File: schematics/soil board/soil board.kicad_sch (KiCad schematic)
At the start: 20 parts, among them J1 AVR-ISP-6, U1 ATtiny841-SS, U3 MCP9700Ax-ETT

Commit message: rough draft for a board with capcitive sensor and soil temp sensor, can use rs-485 to communicate
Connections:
- net floating is gone; now on net CAP_CHARGE: Elecctrodes1.2
- net CAP_CHARGE: no longer Elecctrodes1.1
- net GND: now also Elecctrodes1.1
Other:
- moved on the sheet: Elecctrodes1
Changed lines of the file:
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@@
-	(wire
-		(pts
-			(xy 162.56 85.09) (xy 168.91 85.09)
-		)
-		(stroke
-			(width 0)
-			(type default)
-		)
-	)
 	(wire
 		(pts
@@
 		(property "Intersheetrefs" "${INTERSHEET_REFS}"
 			(at 98.0537 107.95 0)
-			(hide yes)
-			(show_name no)
-			(do_not_autoplace no)
-			(effects
-				(font
-					(size 1.27 1.27)
-				)
-				(justify left)
-			)
-		)
-	)
-	(global_label "floating"
-		(shape input)
-		(at 168.91 85.09 0)
-		(fields_autoplaced yes)
-		(effects
-			(font
-				(size 1.27 1.27)
-			)
-			(justify left)
-		)
-		(property "Intersheetrefs" "${INTERSHEET_REFS}"
-			(at 179.2126 85.09 0)
 			(hide yes)
 			(show_name no)
@@
 	(symbol
 		(lib_id "Device:C")
-		(at 158.75 85.09 90)
+		(at 158.75 85.09 270)
 		(unit 1)
 		(body_style 1)
@@
 		)
 		(property "Footprint" "soil_cap:Untitled"
-			(at 162.56 84.1248 0)
+			(at 154.94 86.0552 0)
 			(hide yes)
 			(show_name no)
@@
 					(unit 1)
 				)
+			)
+		)
+	)
+	(symbol
+		(lib_id "power:GND")
+		(at 162.56 85.09 0)
+		(unit 1)
+		(body_style 1)
+		(exclude_from_sim no)
+		(in_bom yes)
+		(on_board yes)
+		(in_pos_files yes)
+		(dnp no)
+		(fields_autoplaced yes)
+		(property "Reference" "#PWR09"
+			(at 162.56 91.44 0)
+			(hide yes)
+			(show_name no)
+			(do_not_autoplace no)
+			(effects
+				(font
+					(size 1.27 1.27)
+				)
+			)
+		)
+		(property "Value" "GND"
+			(at 162.56 90.17 0)
+			(show_name no)
+			(do_not_autoplace no)
+			(effects
+				(font
+					(size 1.27 1.27)
+				)
+			)
+		)
+		(property "Footprint" ""
+			(at 162.56 85.09 0)
+			(hide yes)
+			(show_name no)
+			(do_not_autoplace no)
+			(effects
+				(font
+					(size 1.27 1.27)
+				)
+			)
+		)
+		(property "Datasheet" ""
+			(at 162.56 85.09 0)
+			(hide yes)
+			(show_name no)
+			(do_not_autoplace no)
+			(effects
+				(font
+					(size 1.27 1.27)
+				)
+			)
+		)
+		(property "Description" "Power symbol creates a global label with name \"GND\" , ground"
+			(at 162.56 85.09 0)
+			(hide yes)
+			(show_name no)
+			(do_not_autoplace no)
+			(effects
+				(font
+					(size 1.27 1.27)
+				)
+			)
+		)
+		(pin "1"
+		)
+		(instances
+			(project "soil board"
+				(path "/37916b7e-9322-4a41-838c-6f1f6ef59153"
+					(reference "#PWR09")
+					(unit 1)
+				)

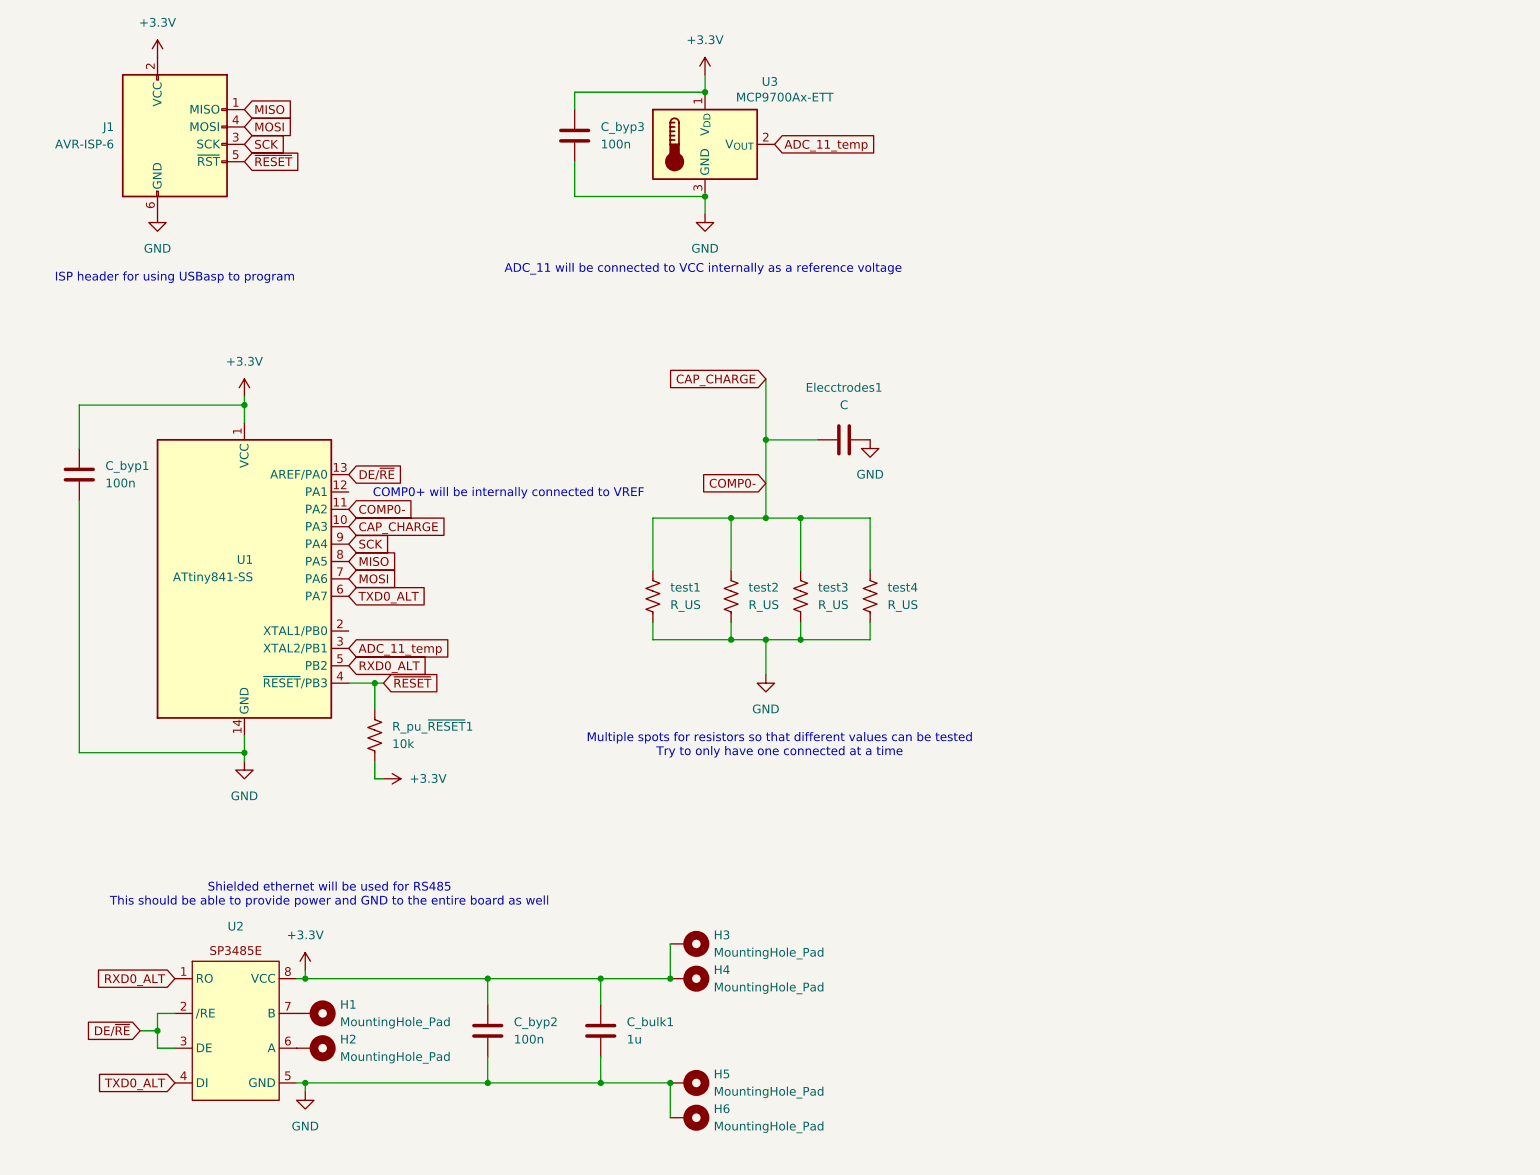
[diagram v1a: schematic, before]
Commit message: Changed connectors for rs-485
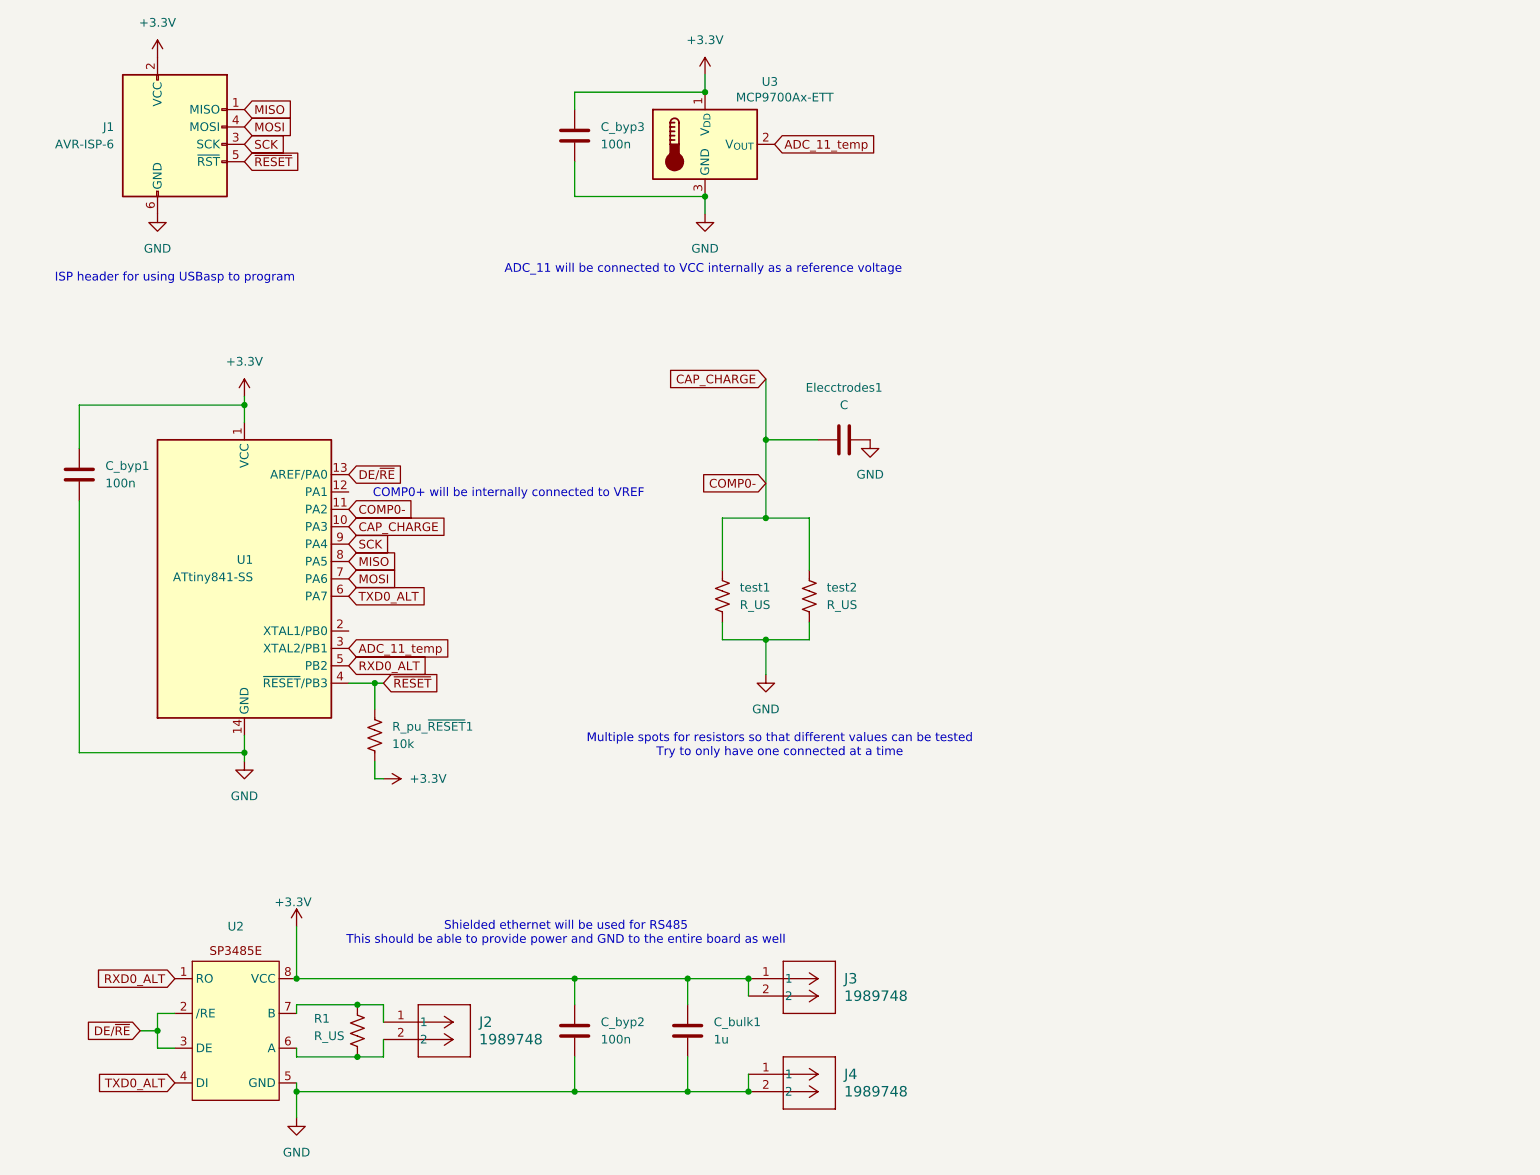
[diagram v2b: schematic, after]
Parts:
- removed H1, H2, H3, H4, H5, H6: MountingHole_Pad, Connector_Wire:SolderWire-0.5sqmm_1x01_D0.9mm_OD2.1mm, symbol Mechanical:MountingHole_Pad
- removed test3, test4: R_US, Resistor_THT:R_Axial_DIN0207_L6.3mm_D2.5mm_P7.62mm_Horizontal, symbol Device:R_US
- added J2: 1989748, footprints:CONN_1989748_PXC, symbol 2026-10-16_21-18-38:1989748
- added J3, J4: 1989748, CONN_1989748_PXC, symbol 2026-10-16_21-18-38:1989748
- added R1: R_US, Resistor_SMD:R_0805_2012Metric_Pad1.20x1.40mm_HandSolder, symbol Device:R_US
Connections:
- net +3.3V: now also J3.1, J3.2
- net GND: now also J4.1, J4.2
- net at U2.7 (B): now also J2.1, R1.1
- net at U2.6 (A): now also J2.2, R1.2
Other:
- moved on the sheet: C_bulk1, C_byp2, test1, test2

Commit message: Interface for temp sensor and soil moisture sensor
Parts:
- removed Elecctrodes1: C, soil_cap:Untitled, symbol Device:C
- removed J2: 1989748, footprints:CONN_1989748_PXC, symbol 2026-10-16_21-18-38:1989748
- removed J3, J4: 1989748, CONN_1989748_PXC, symbol 2026-10-16_21-18-38:1989748
- removed test1, test2: R_US, Resistor_THT:R_Axial_DIN0207_L6.3mm_D2.5mm_P7.62mm_Horizontal, symbol Device:R_US
- added J2: Conn_01x03_Pin, Connector_PinHeader_2.54mm:PinHeader_1x03_P2.54mm_Vertical, symbol Connector:Conn_01x03_Pin
- added J5: 54602-908LF, CONN8_2-908LF_AMP, symbol 2026-10-21_23-02-14:54602-908LF
- added PWR1, TEST1: LED, LED_SMD:LED_0805_2012Metric_Pad1.15x1.40mm_HandSolder, symbol Device:LED
- added R2, R3: 56, Resistor_SMD:R_0805_2012Metric_Pad1.20x1.40mm_HandSolder, symbol Device:R_US
- R1: value R_US -> 120
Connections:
- net +3.3V: now also J2.3 (Pin_3), J5.7, J5.8, PWR1.2 (A)
- net ADC_11_temp: now also U1.2 (XTAL1/PB0); no longer U1.3 (XTAL2/PB1)
- net GND: now also J2.1 (Pin_1), J5.1, J5.2, R2.2, R3.2
- net /RE: now reaches U1.12 (PA1)
- net /RE: now also U2.2 (/RE)
- net at R1.2, U2.6 (A): now also J5.4
- net at R1.1, U2.7 (B): now also J5.5
- net CAP_CHARGE: no longer names the net of U1.11 (PA2)
- net CAP_CHARGE: now also TEST1.2 (A); no longer U1.10 (PA3)
- net DE/~{RE} renamed DE
- net DE: no longer U2.2 (/RE)
- new net: PWR1.1 (K), R2.1
- new net: R3.1, TEST1.1 (K)
- new net ADC_10_moisture: J2.2 (Pin_2), U1.3 (XTAL2/PB1)
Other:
- note added: "Interface with soil moisture Sensor"
- note added: "Place near the RJ45 jack"
- note removed: "COMP0+ will be internally connected to VREF"
- note removed: "Multiple spots for resistors so that different values can be tested Try to only have one connected at a time"
- moved on the sheet: C_bulk1, C_byp1, C_byp2, R1, R_pu_~{RESET}1, U1, U2

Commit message: Final changes to pcbs before ordering
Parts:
- renumbered C_bulk1 to C1, C_byp1 to C2, C_byp2 to C3, C_byp3 to C4, J5 to J2, J2 to J3, R_pu_~{RESET}1 to R1, R3 to R2, R2 to R3, R1 to R4
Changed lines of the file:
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@@
 		(in_pos_files yes)
 		(dnp no)
-		(property "Reference" "R2"
+		(property "Reference" "R3"
 			(at 166.37 134.112 0)
 			(show_name no)
@@
 			(project "soil board"
 				(path "/37916b7e-9322-4a41-838c-6f1f6ef59153"
-					(reference "R2")
+					(reference "R3")
 					(unit 1)
 				)
@@
 		(dnp no)
 		(fields_autoplaced yes)
-		(property "Reference" "R_pu_~{RESET}1"
+		(property "Reference" "R1"
 			(at 88.9 132.0799 0)
 			(show_name no)
@@
 			(project "soil board"
 				(path "/37916b7e-9322-4a41-838c-6f1f6ef59153"
-					(reference "R_pu_~{RESET}1")
+					(reference "R1")
 					(unit 1)
 				)
@@
 		(in_pos_files yes)
 		(dnp no)
-		(property "Reference" "C_byp2"
+		(property "Reference" "C3"
 			(at 133.35 90.1699 0)
 			(show_name no)
@@
 			(project "soil board"
 				(path "/37916b7e-9322-4a41-838c-6f1f6ef59153"
-					(reference "C_byp2")
+					(reference "C3")
 					(unit 1)
 				)
@@
 		(dnp no)
 		(fields_autoplaced yes)
-		(property "Reference" "C_bulk1"
+		(property "Reference" "C1"
 			(at 190.5 129.5399 0)
 			(show_name no)
@@
 			(project "soil board"
 				(path "/37916b7e-9322-4a41-838c-6f1f6ef59153"
-					(reference "C_bulk1")
+					(reference "C1")
 					(unit 1)
 				)
@@
 		(dnp no)
 		(fields_autoplaced yes)
-		(property "Reference" "J2"
+		(property "Reference" "J3"
 			(at 133.35 119.3799 0)
 			(show_name no)
@@
 			(project "soil board"
 				(path "/37916b7e-9322-4a41-838c-6f1f6ef59153"
-					(reference "J2")
+					(reference "J3")
 					(unit 1)
 				)
@@
 		(in_pos_files yes)
 		(dnp no)
-		(property "Reference" "R3"
+		(property "Reference" "R2"
 			(at 100.33 102.362 0)
 			(show_name no)
@@
 			(project "soil board"
 				(path "/37916b7e-9322-4a41-838c-6f1f6ef59153"
-					(reference "R3")
+					(reference "R2")
 					(unit 1)
 				)
@@
 		(dnp no)
 		(fields_autoplaced yes)
-		(property "Reference" "C_byp3"
+		(property "Reference" "C4"
 			(at 123.19 39.3699 0)
 			(show_name no)
@@
 			(project "soil board"
 				(path "/37916b7e-9322-4a41-838c-6f1f6ef59153"
-					(reference "C_byp3")
+					(reference "C4")
 					(unit 1)
 				)
@@
 		(dnp no)
 		(fields_autoplaced yes)
-		(property "Reference" "J5"
+		(property "Reference" "J2"
 			(at 228.6 88.8999 0)
 			(show_name no)
@@
 			(project "soil board"
 				(path "/37916b7e-9322-4a41-838c-6f1f6ef59153"
-					(reference "J5")
+					(reference "J2")
 					(unit 1)
 				)
@@
 		(dnp no)
 		(fields_autoplaced yes)
-		(property "Reference" "C_byp1"
+		(property "Reference" "C2"
 			(at 46.99 93.9799 0)
 			(show_name no)
@@
 			(project "soil board"
 				(path "/37916b7e-9322-4a41-838c-6f1f6ef59153"
-					(reference "C_byp1")
+					(reference "C2")
 					(unit 1)
 				)
@@
 		(in_pos_files yes)
 		(dnp no)
-		(property "Reference" "R1"
+		(property "Reference" "R4"
 			(at 175.26 89.662 0)
 			(show_name no)
@@
 			(project "soil board"
 				(path "/37916b7e-9322-4a41-838c-6f1f6ef59153"
-					(reference "R1")
-					(unit 1)
-				)
+					(reference "R4")
+					(unit 1)
+				)
